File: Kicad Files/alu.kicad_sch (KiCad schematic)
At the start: 27 parts, among them U47 74LS245, U48 74LS283, U49 74LS283, U50 74LS86, U51 74LS86

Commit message: alu rework start
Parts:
- added U? (x2): SST39SF020, symbol Memory_Flash:SST39SF020
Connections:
- net GND: now also U?.16 (GND), U?.16 (GND)
- net VCC: now also U?.31 (PGM), U?.31 (PGM), U?.32 (VCC), U?.32 (VCC)
- new net: U?.10 (A2), U?.10 (A2)
- new net: U?.11 (A1), U?.11 (A1)
- new net: U?.12 (A0), U?.12 (A0)
- new net: U?.2 (A16), U?.2 (A16)
- new net: U?.22 (CE), U?.24 (OE) (x2)
- new net: U?.23 (A10), U?.23 (A10)
- new net: U?.25 (A11), U?.25 (A11)
- new net: U?.26 (A9), U?.26 (A9)
- new net: U?.27 (A8), U?.27 (A8)
- new net: U?.28 (A13), U?.28 (A13)
- new net: U?.29 (A14), U?.29 (A14)
- new net: U?.3 (A15), U?.3 (A15)
- new net: U?.30 (A17), U?.30 (A17)
- new net: U?.4 (A12), U?.4 (A12)
- new net: U?.5 (A7), U?.5 (A7)
- new net: U?.6 (A6), U?.6 (A6)
- new net: U?.7 (A5), U?.7 (A5)
- new net: U?.8 (A4), U?.8 (A4)
- new net: U?.9 (A3), U?.9 (A3)
- new net CF: U?.13 (D0)
- new net NF: U?.17 (D3)
- new net OF: U?.14 (D1)
- new net ZF: U?.15 (D2)
- new net Σ_0: U?.13 (D0)
- new net Σ_1: U?.14 (D1)
- new net Σ_2: U?.15 (D2)
- new net Σ_3: U?.17 (D3)
- new net Σ_4: U?.18 (D4)
- new net Σ_5: U?.19 (D5)
- new net Σ_6: U?.20 (D6)
- new net Σ_7: U?.21 (D7)
- no-connect marks 0 -> 6
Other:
- moved on the sheet: C21, C22, D139, D140, D141, D142, D143, D144, D145, D146, D147, D148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

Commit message: np3
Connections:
- net BUS_0: now also U?.13 (D0); no longer U47.11 (B7)
- net BUS_1: now also U?.14 (D1); no longer U47.12 (B6)
- net BUS_2: now also U?.15 (D2); no longer U47.13 (B5)
- net BUS_3: now also U?.17 (D3); no longer U47.14 (B4)
- net BUS_4: now also U?.18 (D4); no longer U47.15 (B3)
- net BUS_5: now also U?.19 (D5); no longer U47.16 (B2)
- net BUS_6: now also U?.20 (D6); no longer U47.17 (B1)
- net BUS_7: now also U?.21 (D7); no longer U47.18 (B0)
- net Σ_0: no longer U?.13 (D0)
- net Σ_1: no longer U?.14 (D1)
- net Σ_2: no longer U?.15 (D2)
- net Σ_3: no longer U?.17 (D3)
- net Σ_4: no longer U?.18 (D4)
- net Σ_5: no longer U?.19 (D5)
- net Σ_6: no longer U?.20 (D6)
- net Σ_7: no longer U?.21 (D7)
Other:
- moved on the sheet: C21, C22, D139, D140, D141, D142, D143, D144, D145, D146, D147, D148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

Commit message: np5
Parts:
- removed C21, C22: C, Capacitor_THT:C_Disc_D4.3mm_W1.9mm_P5.00mm, symbol Device:C
- removed D139, D140, D141, D142, D143, D144, D145, D146, D147, D148: LED, symbol Device:LED
- removed R148, R149, R150, R151, R152, R153, R154, R155, R156, R157: R_Small, symbol Device:R_Small
- removed U47: 74LS245, Package_DIP:DIP-20_W7.62mm, symbol 8bit-computer-rescue:74LS245-8bit-computer-rescue
- removed U48, U49: 74LS283, Package_DIP:DIP-16_W7.62mm, symbol 8bit-computer-rescue:74LS283-8bit-computer-rescue
- removed U50, U51: 74LS86, Package_DIP:DIP-14_W7.62mm, symbol 8bit-computer-rescue:74LS86-8bit-computer-rescue
- removed U? (x2): SST39SF020, symbol Memory_Flash:SST39SF020
- added D? (x12): LED, symbol Device:LED
- added R? (x12): R_Small, symbol Device:R_Small
- added U?: 74LS173, symbol 74xx:74LS173
- added U? (x2): SST39SF040, symbol Memory_Flash:SST39SF040
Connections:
- net A_0: now also U?.12 (A0), U?.12 (A0)
- net A_1: now also U?.11 (A1), U?.11 (A1)
- net A_2: now also U?.10 (A2), U?.10 (A2)
- net A_3: now also U?.9 (A3), U?.9 (A3)
- net A_4: now also U?.8 (A4), U?.8 (A4)
- net A_5: now also U?.7 (A5), U?.7 (A5)
- net A_6: now also U?.6 (A6), U?.6 (A6)
- net A_7: now also U?.5 (A7), U?.5 (A7)
- net BUS_0: now also D?.2 (A), U?.13 (D0)
- net BUS_1: now also D?.2 (A), U?.14 (D1)
- net BUS_2: now also D?.2 (A), U?.15 (D2)
- net BUS_3: now also D?.2 (A), U?.17 (D3)
- net BUS_4: now also D?.2 (A), U?.18 (D4)
- net BUS_5: now also D?.2 (A), U?.19 (D5)
- net BUS_6: now also D?.2 (A), U?.20 (D6)
- net BUS_7: now also D?.2 (A), U?.21 (D7)
- net B_0: now also U?.27 (A8), U?.27 (A8)
- net B_1: now also U?.26 (A9), U?.26 (A9)
- net B_2: now also U?.23 (A10), U?.23 (A10)
- net B_3: now also U?.25 (A11), U?.25 (A11)
- net B_4: now also U?.4 (A12), U?.4 (A12)
- net B_5: now also U?.28 (A13), U?.28 (A13)
- net B_6: now also U?.29 (A14), U?.29 (A14)
- net B_7: now also U?.3 (A15), U?.3 (A15)
- net CF: now also D?.2 (A), U?.3 (Q0)
- net GND: now also R?.2, R?.2, R?.2, R?.2, R?.2, R?.2, R?.2, R?.2, R?.2, R?.2, R?.2, R?.2, U?.1 (Oe1), U?.16 (GND), U?.16 (GND), U?.2 (Oe2), U?.8 (GND)
- net NF: now also D?.2 (A), U?.6 (Q3)
- net OF: now also D?.2 (A), U?.4 (Q1)
- net VCC: now also U?.16 (VCC), U?.31 (PGM), U?.31 (PGM), U?.32 (VCC), U?.32 (VCC)
- net ZF: now also D?.2 (A), U?.5 (Q2)
- net ~{ΣO}: now also U?.22 (CE), U?.22 (CE), U?.24 (OE), U?.24 (OE)
- net Σ_0: now also U?.1 (A18), U?.1 (A18), U?.2 (A16), U?.2 (A16), U?.30 (A17), U?.30 (A17)
- new net: D?.1 (K), R?.1 (x12)
- new net: U?.11 (D3), U?.17 (D3)
- new net: U?.12 (D2), U?.15 (D2)
- new net: U?.13 (D1), U?.14 (D1)
- new net: U?.13 (D0), U?.14 (D0)
- new net CLK: U?.7 (Cp)
- new net CLR: U?.15 (Mr)
- new net ~{FI}: U?.10 (E2), U?.9 (E1)
- no-connect marks 6 -> 4

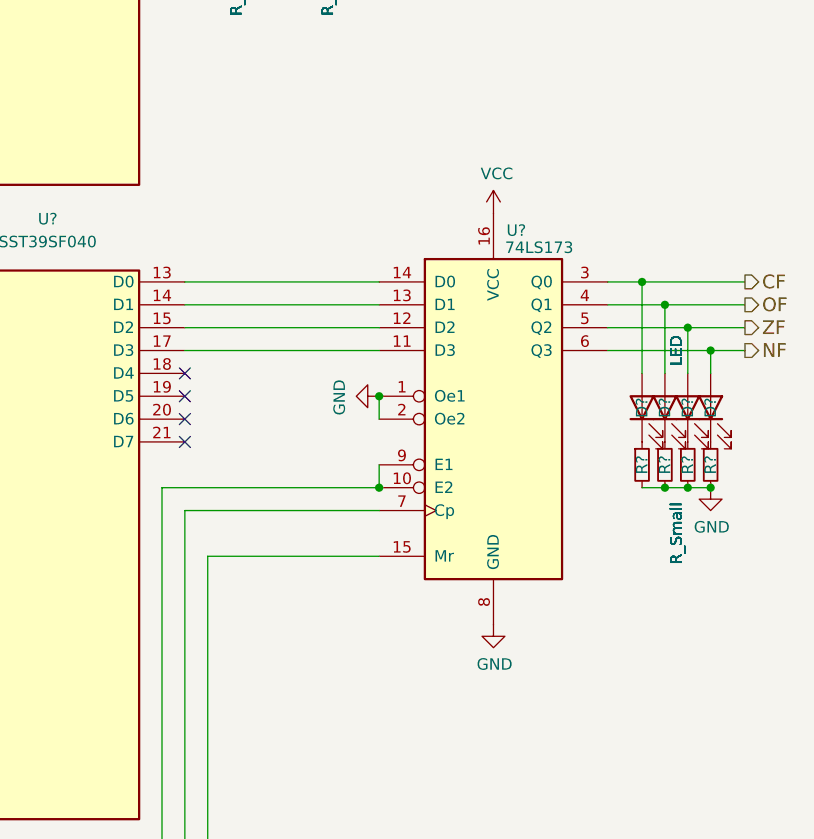
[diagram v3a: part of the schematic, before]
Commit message: added Flachband
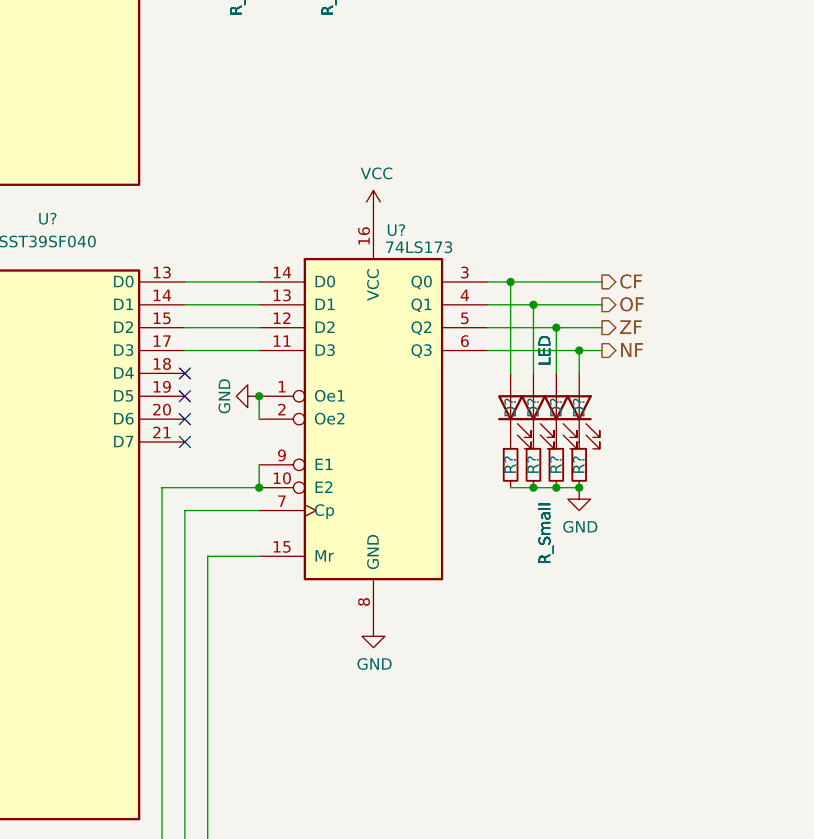
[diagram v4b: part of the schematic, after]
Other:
- moved on the sheet: D?, R?, U?

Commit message: tidy up
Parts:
- gave numbers to parts that had none: 27
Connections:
- net Σ_0: no longer U40.1 (A18), U40.30 (A17), U41.1 (A18), U41.30 (A17)
- new net Σ_1: U40.30 (A17), U41.30 (A17)
- new net Σ_2: U40.1 (A18), U41.1 (A18)

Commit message: updated library
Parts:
- renumbered D123 to D131, D124 to D132, D125 to D133, D126 to D134, D127 to D135, D128 to D136, D129 to D137, D130 to D138, D131 to D139, D132 to D140, D133 to D141, D134 to D142, R132 to R140, R133 to R141, R134 to R142, R135 to R143, R136 to R144, R137 to R145, R138 to R146, R139 to R147, R140 to R148, R141 to R149, R142 to R150, R143 to R151

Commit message: im sooo stupiiid
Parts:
- added U43, U44: 74HC245, symbol 74xx:74HC245
- renumbered D139 to D138, D138 to D139, R148 to R147, R147 to R148
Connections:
- net OF is gone; now on net NF: D140.2 (A), U42.4 (Q1)
- net BUS_0: now also U43.18 (B0), U44.18 (B0); no longer D131.2 (A), U40.13 (D0)
- net BUS_1: now also U43.17 (B1), U44.17 (B1); no longer D132.2 (A), U40.14 (D1)
- net BUS_2: now also U43.16 (B2), U44.16 (B2); no longer D133.2 (A), U40.15 (D2)
- net BUS_3: now also U43.15 (B3), U44.15 (B3); no longer D134.2 (A), U40.17 (D3)
- net BUS_4: now also U43.14 (B4), U44.14 (B4); no longer D135.2 (A), U40.18 (D4)
- net BUS_5: now also U43.13 (B5), U44.13 (B5); no longer D136.2 (A), U40.19 (D5)
- net BUS_6: now also U43.12 (B6), U44.12 (B6); no longer D137.2 (A), U40.20 (D6)
- net BUS_7: now also U43.11 (B7), U44.11 (B7); no longer D139.2 (A), U40.21 (D7)
- net CF: now also D141.2 (A), U42.5 (Q2), U44.4 (A2); no longer D138.2 (A), U42.3 (Q0)
- net GND: now also U40.22 (CE), U40.24 (OE), U41.22 (CE), U41.24 (OE), U43.10 (GND), U44.10 (GND), U44.6 (A4), U44.7 (A5), U44.8 (A6), U44.9 (A7)
- net NF: now also U44.3 (A1); no longer D142.2 (A), U42.6 (Q3)
- net VCC: now also U43.1 (A->B), U43.20 (VCC), U44.1 (A->B), U44.20 (VCC)
- net ZF: now also D138.2 (A), U42.3 (Q0), U44.2 (A0); no longer D141.2 (A), U42.5 (Q2)
- net ~{ΣO}: now also U44.19 (CE); no longer U40.22 (CE), U40.24 (OE), U41.22 (CE), U41.24 (OE)
- new net: D133.2 (A), U40.15 (D2), U43.4 (A2)
- new net: D136.2 (A), U40.19 (D5), U43.7 (A5)
- new net: D131.2 (A), U40.13 (D0), U43.2 (A0)
- new net: D134.2 (A), U40.17 (D3), U43.5 (A3)
- new net: D139.2 (A), U40.21 (D7), U43.9 (A7)
- new net: D132.2 (A), U40.14 (D1), U43.3 (A1)
- new net: D135.2 (A), U40.18 (D4), U43.6 (A4)
- new net: D137.2 (A), U40.20 (D6), U43.8 (A6)
- new net BF: D142.2 (A), U42.6 (Q3), U44.5 (A3)
- new net ~{FO}: U43.19 (CE)
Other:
- moved on the sheet: D131, D132, D133, D134, D135, D136, D137, D138, D139, D140, D141, D142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

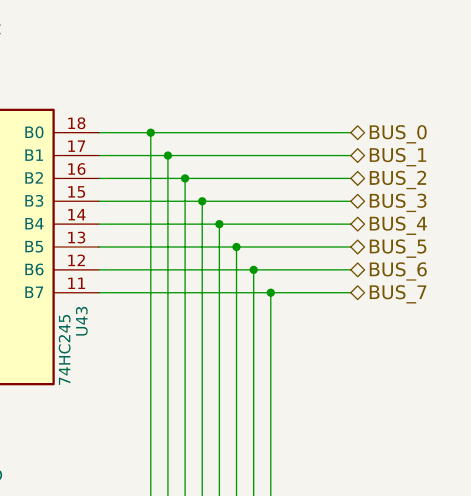
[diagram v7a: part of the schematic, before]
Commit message: complete redraw to bus system
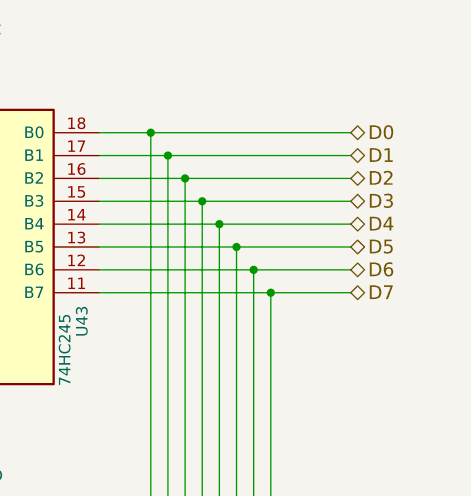
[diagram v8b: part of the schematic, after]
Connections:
- net BUS_0 renamed D0
- net BUS_1 renamed D1
- net BUS_2 renamed D2
- net BUS_3 renamed D3
- net BUS_4 renamed D4
- net BUS_5 renamed D5
- net BUS_6 renamed D6
- net BUS_7 renamed D7
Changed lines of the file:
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@@
-    (effects (font (size 1.524 1.524)) (justify left))
-  )
-  (hierarchical_label "BUS_3" (shape tri_state) (at 236.855 43.815 0)
-    (effects (font (size 1.524 1.524)) (justify left))
-  )
-  (hierarchical_label "BUS_0" (shape tri_state) (at 236.855 36.195 0)
-    (effects (font (size 1.524 1.524)) (justify left))
-  )
-  (hierarchical_label "BUS_6" (shape tri_state) (at 236.855 51.435 0)
     (effects (font (size 1.524 1.524)) (justify left))
   )
@@
     (effects (font (size 1.524 1.524)) (justify right))
   )
+  (hierarchical_label "D3" (shape tri_state) (at 236.855 43.815 0)
+    (effects (font (size 1.524 1.524)) (justify left))
+  )
   (hierarchical_label "BF" (shape output) (at 167.64 99.695 90)
     (effects (font (size 1.524 1.524)) (justify left))
@@
     (effects (font (size 1.524 1.524)) (justify right))
   )
-  (hierarchical_label "BUS_1" (shape tri_state) (at 236.855 38.735 0)
-    (effects (font (size 1.524 1.524)) (justify left))
-  )
   (hierarchical_label "A_7" (shape input) (at 45.085 124.46 180)
     (effects (font (size 1.524 1.524)) (justify right))
-  )
-  (hierarchical_label "BUS_2" (shape tri_state) (at 236.855 41.275 0)
-    (effects (font (size 1.524 1.524)) (justify left))
   )
   (hierarchical_label "B_5" (shape input) (at 45.085 139.7 180)
     (effects (font (size 1.524 1.524)) (justify right))
   )
-  (hierarchical_label "BUS_5" (shape tri_state) (at 236.855 48.895 0)
+  (hierarchical_label "D7" (shape tri_state) (at 236.855 53.975 0)
+    (effects (font (size 1.524 1.524)) (justify left))
+  )
+  (hierarchical_label "D4" (shape tri_state) (at 236.855 46.355 0)
     (effects (font (size 1.524 1.524)) (justify left))
   )
   (hierarchical_label "~{FI}" (shape input) (at 236.855 165.1 0)
+    (effects (font (size 1.524 1.524)) (justify left))
+  )
+  (hierarchical_label "D1" (shape tri_state) (at 236.855 38.735 0)
+    (effects (font (size 1.524 1.524)) (justify left))
+  )
+  (hierarchical_label "D2" (shape tri_state) (at 236.855 41.275 0)
+    (effects (font (size 1.524 1.524)) (justify left))
+  )
+  (hierarchical_label "D0" (shape tri_state) (at 236.855 36.195 0)
     (effects (font (size 1.524 1.524)) (justify left))
   )
@@
   (hierarchical_label "B_2" (shape input) (at 45.085 132.08 180)
     (effects (font (size 1.524 1.524)) (justify right))
-  )
-  (hierarchical_label "BUS_7" (shape tri_state) (at 236.855 53.975 0)
-    (effects (font (size 1.524 1.524)) (justify left))
   )
   (hierarchical_label "B_3" (shape input) (at 45.085 134.62 180)
@@
     (effects (font (size 1.524 1.524)) (justify right))
   )
-  (hierarchical_label "BUS_4" (shape tri_state) (at 236.855 46.355 0)
-    (effects (font (size 1.524 1.524)) (justify left))
-  )
   (hierarchical_label "~{FO}" (shape input) (at 236.855 162.56 0)
     (effects (font (size 1.524 1.524)) (justify left))
@@
     (effects (font (size 1.524 1.524)) (justify right))
   )
+  (hierarchical_label "D5" (shape tri_state) (at 236.855 48.895 0)
+    (effects (font (size 1.524 1.524)) (justify left))
+  )
   (hierarchical_label "A_4" (shape input) (at 45.085 116.84 180)
     (effects (font (size 1.524 1.524)) (justify right))
@@
     (effects (font (size 1.524 1.524)) (justify right))
   )
+  (hierarchical_label "D6" (shape tri_state) (at 236.855 51.435 0)
+    (effects (font (size 1.524 1.524)) (justify left))
+  )
   (hierarchical_label "ZF" (shape output) (at 160.02 99.695 90)
